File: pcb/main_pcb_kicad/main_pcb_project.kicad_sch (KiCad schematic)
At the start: 0 parts

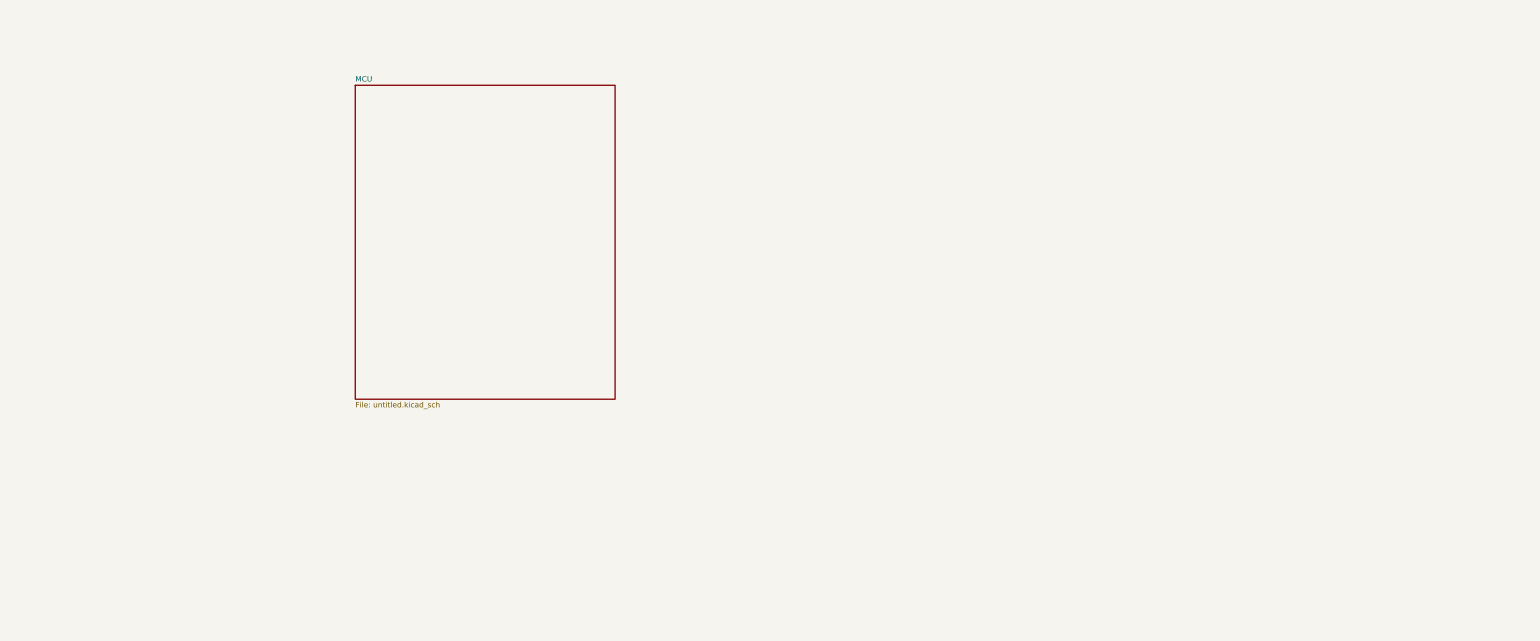
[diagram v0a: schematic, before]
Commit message: Added everything to main schematic
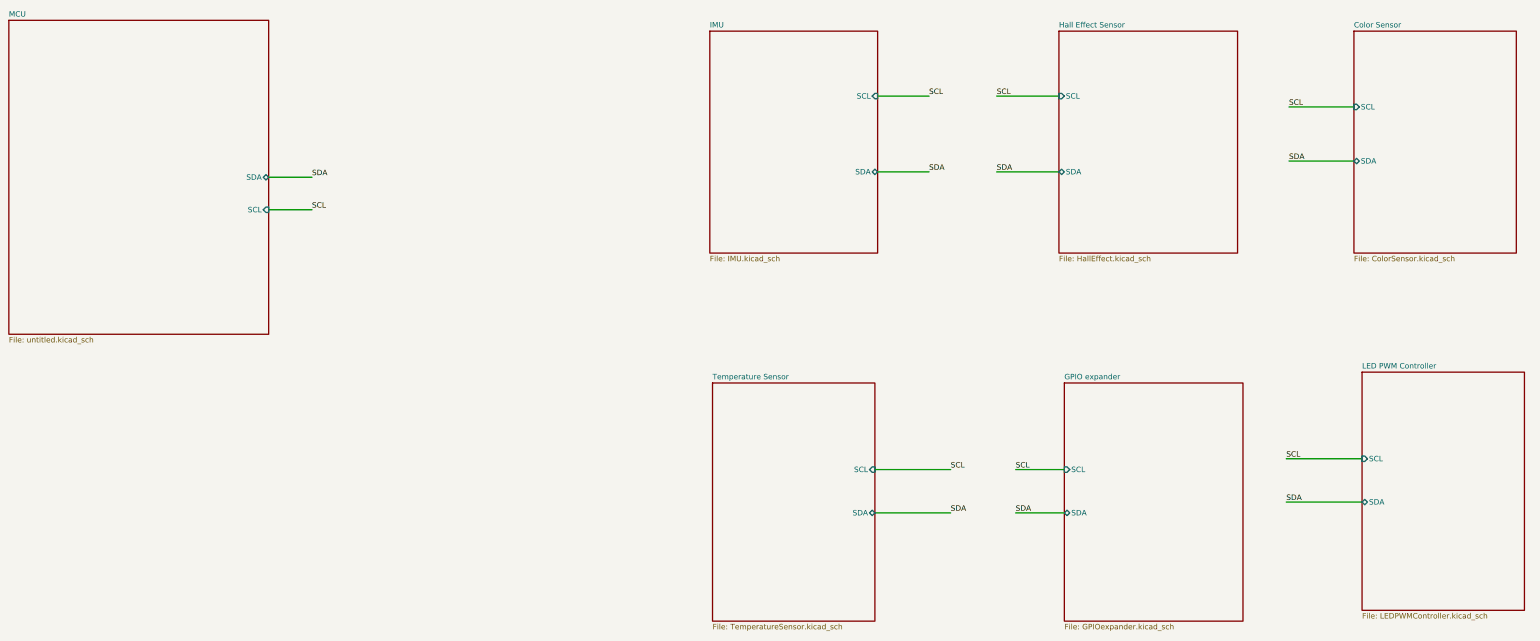
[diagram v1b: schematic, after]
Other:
- added sheet Color Sensor (ColorSensor.kicad_sch)
- added sheet GPIO expander (GPIOexpander.kicad_sch)
- added sheet Hall Effect Sensor (HallEffect.kicad_sch)
- added sheet IMU (IMU.kicad_sch)
- added sheet LED PWM Controller (LEDPWMController.kicad_sch)
- added sheet Temperature Sensor (TemperatureSensor.kicad_sch)
- sheet MCU ports: added SCL, SDA; removed none

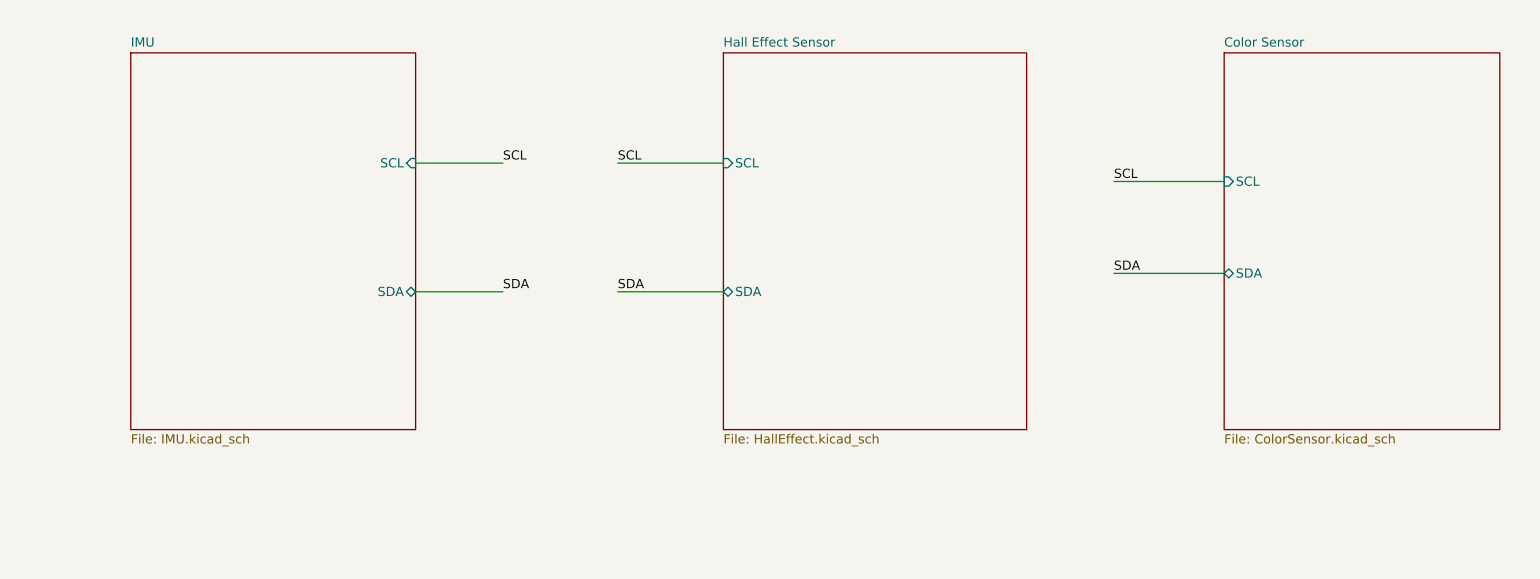
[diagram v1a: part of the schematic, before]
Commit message: Adding footprints
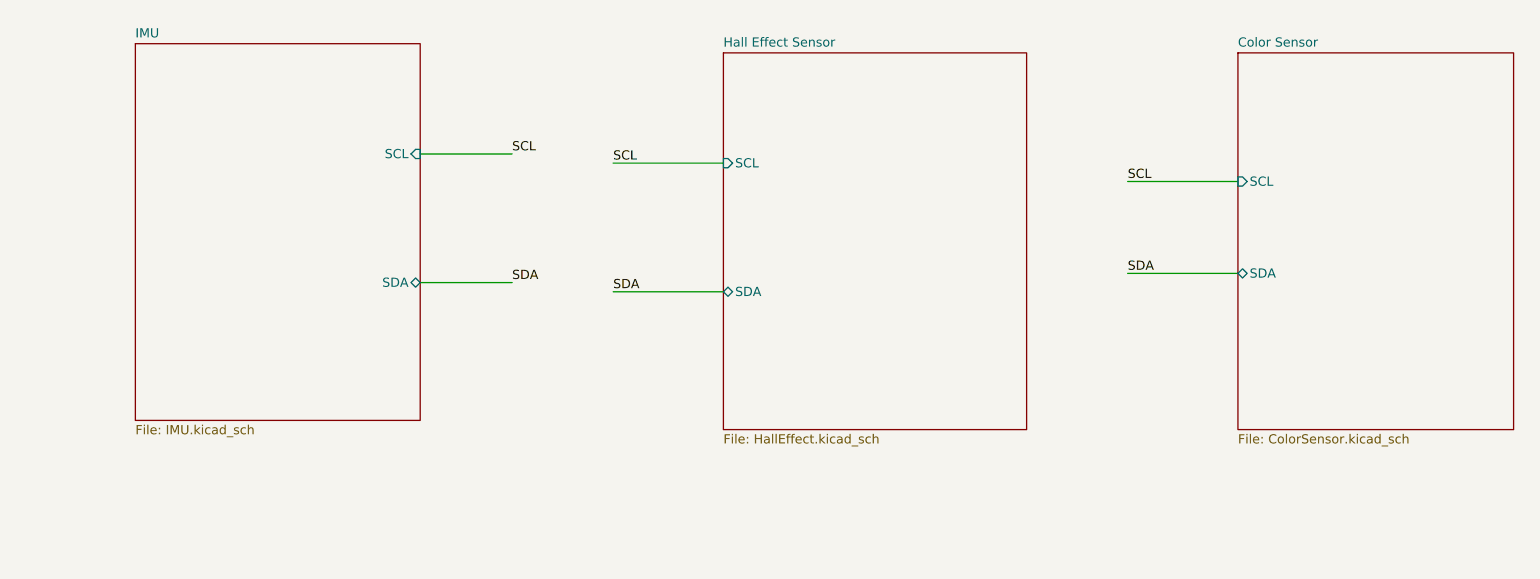
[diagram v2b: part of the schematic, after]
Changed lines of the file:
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@@
 	(wire
 		(pts
-			(xy 329.565 59.69) (xy 344.805 59.69)
-		)
-		(stroke
-			(width 0)
-			(type default)
-		)
-	)
-	(wire
-		(pts
-			(xy 260.985 44.45) (xy 275.59 44.45)
-		)
-		(stroke
-			(width 0)
-			(type default)
-		)
-	)
-	(wire
-		(pts
-			(xy 233.045 44.45) (xy 245.11 44.45)
+			(xy 331.47 59.69) (xy 346.71 59.69)
+		)
+		(stroke
+			(width 0)
+			(type default)
+		)
+	)
+	(wire
+		(pts
+			(xy 260.35 44.45) (xy 275.59 44.45)
+		)
+		(stroke
+			(width 0)
+			(type default)
+		)
+	)
+	(wire
+		(pts
+			(xy 233.68 43.18) (xy 246.38 43.18)
 		)
 		(stroke
@@
 	(wire
 		(pts
-			(xy 233.045 62.23) (xy 245.11 62.23)
-		)
-		(stroke
-			(width 0)
-			(type default)
-		)
-	)
-	(wire
-		(pts
-			(xy 329.565 46.99) (xy 344.805 46.99)
-		)
-		(stroke
-			(width 0)
-			(type default)
-		)
-	)
-	(wire
-		(pts
-			(xy 260.985 62.23) (xy 275.59 62.23)
+			(xy 233.68 60.96) (xy 246.38 60.96)
+		)
+		(stroke
+			(width 0)
+			(type default)
+		)
+	)
+	(wire
+		(pts
+			(xy 331.47 46.99) (xy 346.71 46.99)
+		)
+		(stroke
+			(width 0)
+			(type default)
+		)
+	)
+	(wire
+		(pts
+			(xy 260.35 62.23) (xy 275.59 62.23)
 		)
 		(stroke
@@
 	)
 	(label "SDA"
-		(at 329.565 59.69 0)
+		(at 331.47 59.69 0)
 		(effects
 			(font
@@
 	)
 	(label "SCL"
-		(at 329.565 46.99 0)
+		(at 331.47 46.99 0)
 		(effects
 			(font
@@
 	)
 	(label "SDA"
-		(at 245.11 62.23 0)
+		(at 246.38 60.96 0)
 		(effects
 			(font
@@
 	)
 	(label "SCL"
-		(at 245.11 44.45 0)
+		(at 246.38 43.18 0)
 		(effects
 			(font
@@
 	)
 	(label "SCL"
-		(at 260.985 44.45 0)
+		(at 260.35 44.45 0)
 		(effects
 			(font
@@
 	)
 	(label "SDA"
-		(at 260.985 62.23 0)
+		(at 260.35 62.23 0)
 		(effects
 			(font
@@
 	)
 	(sheet
-		(at 344.805 29.21)
+		(at 346.71 29.21)
 		(size 38.1 52.07)
 		(exclude_from_sim no)
@@
 		)
 		(property "Sheetname" "Color Sensor"
-			(at 344.805 28.4984 0)
+			(at 346.71 28.4984 0)
 			(show_name no)
 			(do_not_autoplace no)
@@
 		)
 		(property "Sheetfile" "ColorSensor.kicad_sch"
-			(at 344.805 81.8646 0)
+			(at 346.71 81.8646 0)
 			(show_name no)
 			(do_not_autoplace no)
@@
 		)
 		(pin "SCL" input
-			(at 344.805 46.99 180)
+			(at 346.71 46.99 180)
 			(effects
 				(font
@@
 		)
 		(pin "SDA" bidirectional
-			(at 344.805 59.69 180)
+			(at 346.71 59.69 180)
 			(effects
 				(font
@@
 	)
 	(sheet
-		(at 193.675 29.21)
+		(at 194.31 27.94)
 		(size 39.37 52.07)
 		(exclude_from_sim no)
@@
 		)
 		(property "Sheetname" "IMU"
-			(at 193.675 28.4984 0)
+			(at 194.31 27.2284 0)
 			(show_name no)
 			(do_not_autoplace no)
@@
 		)
 		(property "Sheetfile" "IMU.kicad_sch"
-			(at 193.675 81.8646 0)
+			(at 194.31 80.5946 0)
 			(show_name no)
 			(do_not_autoplace no)
@@
 		)
 		(pin "SCL" input
-			(at 233.045 44.45 0)
+			(at 233.68 43.18 0)
 			(effects
 				(font
@@
 		)
 		(pin "SDA" bidirectional
-			(at 233.045 62.23 0)
-			(effects
-				(font
+			(at 233.68 60.96 0)
+			(effects
+				(font
